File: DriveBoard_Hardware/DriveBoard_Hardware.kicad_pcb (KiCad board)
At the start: 2 copper layers, 61 x 99.8 mm, 20 parts, among them U1 MAX_3232, U2 MAX_3232, U3 OKI, U4 TM4C129E_Launchpad

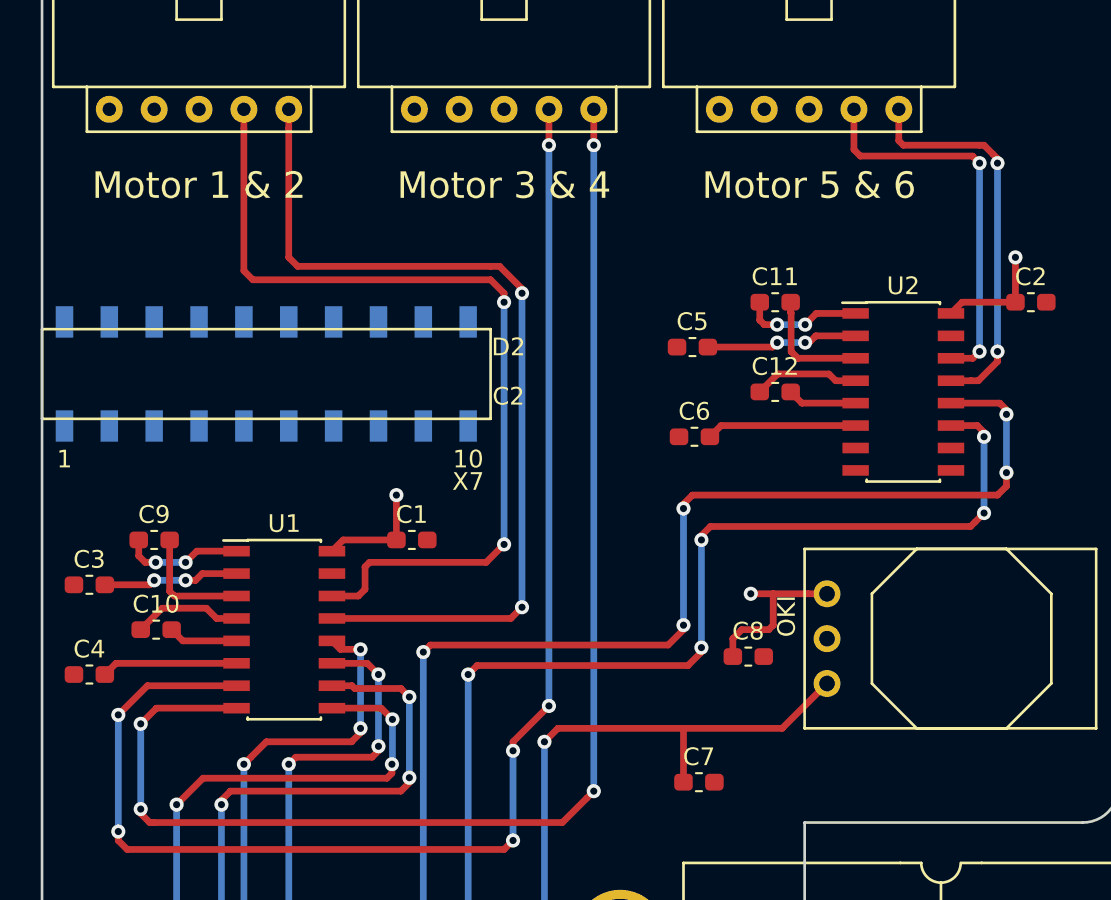
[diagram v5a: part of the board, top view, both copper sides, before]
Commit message: Updated molex pins
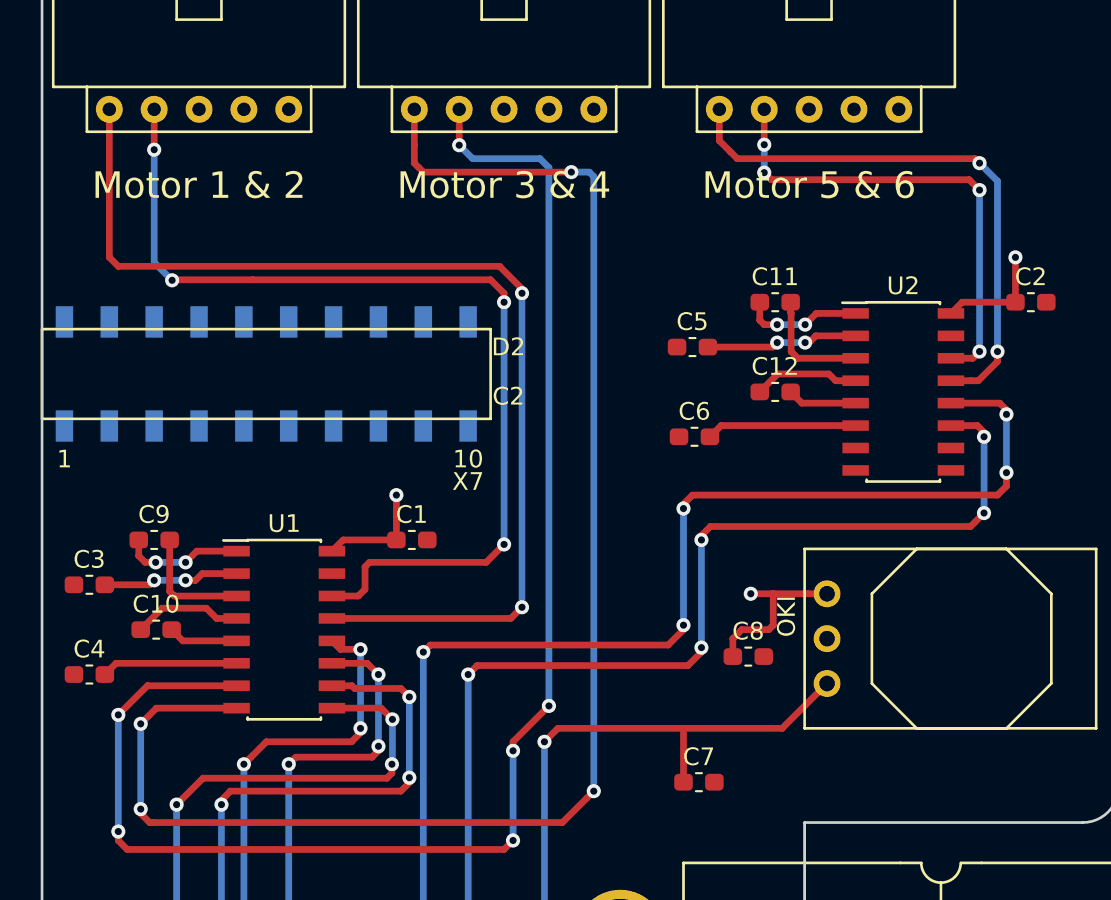
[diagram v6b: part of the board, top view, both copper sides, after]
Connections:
- Conn2 pad 1: Net-(Conn2-Pad1) -> RX_1_SL
- Conn2 pad 2: Net-(Conn2-Pad2) -> TX_1_SL
- Conn2 pad 3: GND -> Net-(Conn2-Pad3)
- Conn2 pad 4: TX_1_SL -> Net-(Conn2-Pad4)
- Conn2 pad 5: RX_1_SL -> GND
- Conn3 pad 1: Net-(Conn3-Pad1) -> RX_2_SL
- Conn3 pad 2: Net-(Conn3-Pad2) -> TX_2_SL
- Conn3 pad 3: GND -> Net-(Conn3-Pad3)
- Conn3 pad 4: TX_2_SL -> Net-(Conn3-Pad4)
- Conn3 pad 5: RX_2_SL -> GND
- Conn4 pad 1: Net-(Conn4-Pad1) -> RX_3_SL
- Conn4 pad 2: Net-(Conn4-Pad2) -> TX_3_SL
- Conn4 pad 3: GND -> Net-(Conn4-Pad3)
- Conn4 pad 4: TX_3_SL -> Net-(Conn4-Pad4)
- Conn4 pad 5: RX_3_SL -> GND
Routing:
- net RX_1_SL: track 51.4 -> 61.5 mm
- net RX_2_SL: track 76.1 -> 85.8 mm
- net RX_3_SL: track 22.4 -> 31.8 mm
- net TX_3_SL: track 22.2 -> 27.1 mm, vias 2 -> 4
- net TX_1_SL: track 50.3 -> 55.1 mm, vias 2 -> 4
- net TX_2_SL: track 79.5 -> 83.8 mm

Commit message: Changing to AP1509
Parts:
- added D1: D_Schottky, Diode_SMD:D_0603_1608Metric_Pad1.05x0.95mm_HandSolder, F.Cu at (201.2, 69.6)
- added D2: LED, LED_SMD:LED_0603_1608Metric_Pad1.05x0.95mm_HandSolder, F.Cu at (197.7, 74.7)
- added D3: LED, LED_SMD:LED_0603_1608Metric_Pad1.05x0.95mm_HandSolder, F.Cu at (199.1, 65.3)
- added D4: LED, LED_SMD:LED_0603_1608Metric_Pad1.05x0.95mm_HandSolder, F.Cu at (191.3, 69.6)
- added D5: LED, LED_SMD:LED_0603_1608Metric_Pad1.05x0.95mm_HandSolder, F.Cu at (209.8, 71.1)
- added L1: 47uH, Inductor_SMD:L_0603_1608Metric_Pad1.05x0.95mm_HandSolder, F.Cu at (208.7, 77.7)
- added R1: 500, LED_SMD:LED_0603_1608Metric_Pad1.05x0.95mm_HandSolder, F.Cu at (192.0, 75.2)
- added R2: 500, LED_SMD:LED_0603_1608Metric_Pad1.05x0.95mm_HandSolder, F.Cu at (208.0, 66.0)
- added R3: 500, LED_SMD:LED_0603_1608Metric_Pad1.05x0.95mm_HandSolder, F.Cu at (203.8, 74.3)
- added R4: 500, LED_SMD:LED_0603_1608Metric_Pad1.05x0.95mm_HandSolder, F.Cu at (214.9, 69.8)
- U3: value OKI -> AP1059
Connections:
- C1 pad 1: +5V -> +3V3
- C2 pad 1: +5V -> +3V3
- C8 pad 1: +5V -> +3V3
- U1 pad 16: +5V -> +3V3
- U2 pad 16: +5V -> +3V3
- U3 pad 2: GND -> Net-(D1-Pad1)
- U3 pad 3: +5V -> +3V3
- U4 pad +3V3: Net-(U4-Pad+3V3) -> +3V3
- U4 pad +5V: +5V -> Net-(U4-Pad+5V)
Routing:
- net +5V: track 23.2 -> 0.00 mm, vias 3 -> 0
- net +3V3: track 0.00 -> 23.2 mm, vias 0 -> 3
- added copper zone on B.Cu, net Net-(U4-Pad+5V)
- removed copper zone on B.Cu, net +5V

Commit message: Updated schematic
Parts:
- U3: footprint MRDT_Devices:OKI_Horizontal -> Package_SO:SOIC-8_3.9x4.9mm_P1.27mm
- moved R2 75.2 mm to (133.5, 56.1), turned to 180 degrees
- moved D3 62.3 mm to (137.5, 56.1), turned to 180 degrees
- moved R3 53.2 mm to (153.6, 56.9), turned to 180 degrees
- moved R4 42.1 mm to (176.3, 53.1), turned to 180 degrees
- moved L1 38.9 mm to (169.8, 80.3), turned to 180 degrees
- moved D4 35.7 mm to (157.8, 56.9), turned to 180 degrees
- moved D5 34.6 mm to (180.2, 53.1), turned to 180 degrees
- moved D2 27.2 mm to (173.6, 87.1), turned to 180 degrees
- moved R1 25.2 mm to (169.8, 87.1), turned to 180 degrees
- moved D1 25.2 mm to (181.5, 85.3)
- moved U3 14.5 mm to (179.3, 79.2), turned to 0 degrees
- moved C8 7.06 mm to (168.0, 84.3), turned to 270 degrees
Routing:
- net +3V3: track 23.2 -> 151.0 mm, vias 3 -> 5
- net RX_2_SL: track 85.8 -> 54.9 mm, vias 4 -> 2
- net TX_2_SL: track 83.8 -> 56.3 mm, vias 6 -> 2
- net Net-(D1-Pad1): track 0.00 -> 18.2 mm
- net /+12V: track 43.2 -> 57.4 mm
- net TX_1_SL: track 55.1 -> 62.7 mm, vias 4 -> 0
- net RX_2_IC: track 41.9 -> 36.5 mm, vias 3 -> 1
- net RX_3_SL: track 31.8 -> 26.6 mm, vias 2 -> 0
- net TX_2_IC: track 43.1 -> 38.0 mm, vias 3 -> 1
- net TX_1_IC: track 30.7 -> 27.9 mm, vias 3 -> 1
- net Net-(D4-Pad2): track 0.00 -> 2.54 mm
- net Net-(D3-Pad2): track 0.00 -> 2.31 mm
- net Net-(D5-Pad2): track 0.00 -> 2.20 mm
- net Net-(D2-Pad2): track 0.00 -> 2.06 mm
- net RX_1_SL: track 61.5 -> 62.6 mm, vias 2 -> 0
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- added copper zone on B.Cu, net GND
- removed copper zone on B.Cu, net Net-(U4-Pad+5V)
